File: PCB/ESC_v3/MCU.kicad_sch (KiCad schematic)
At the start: 40 parts, among them J10 Conn_01x01_Pin, J3 Conn_01x01_Pin, J4 Conn_01x01_Pin, J5 Conn_01x01_Pin, J6 Conn_01x01_Pin, J7 Conn_01x01_Pin, J8 Conn_01x01_Pin, J9 Conn_01x01_Pin, U5 STM32G431CBTx, Y2 16MHz

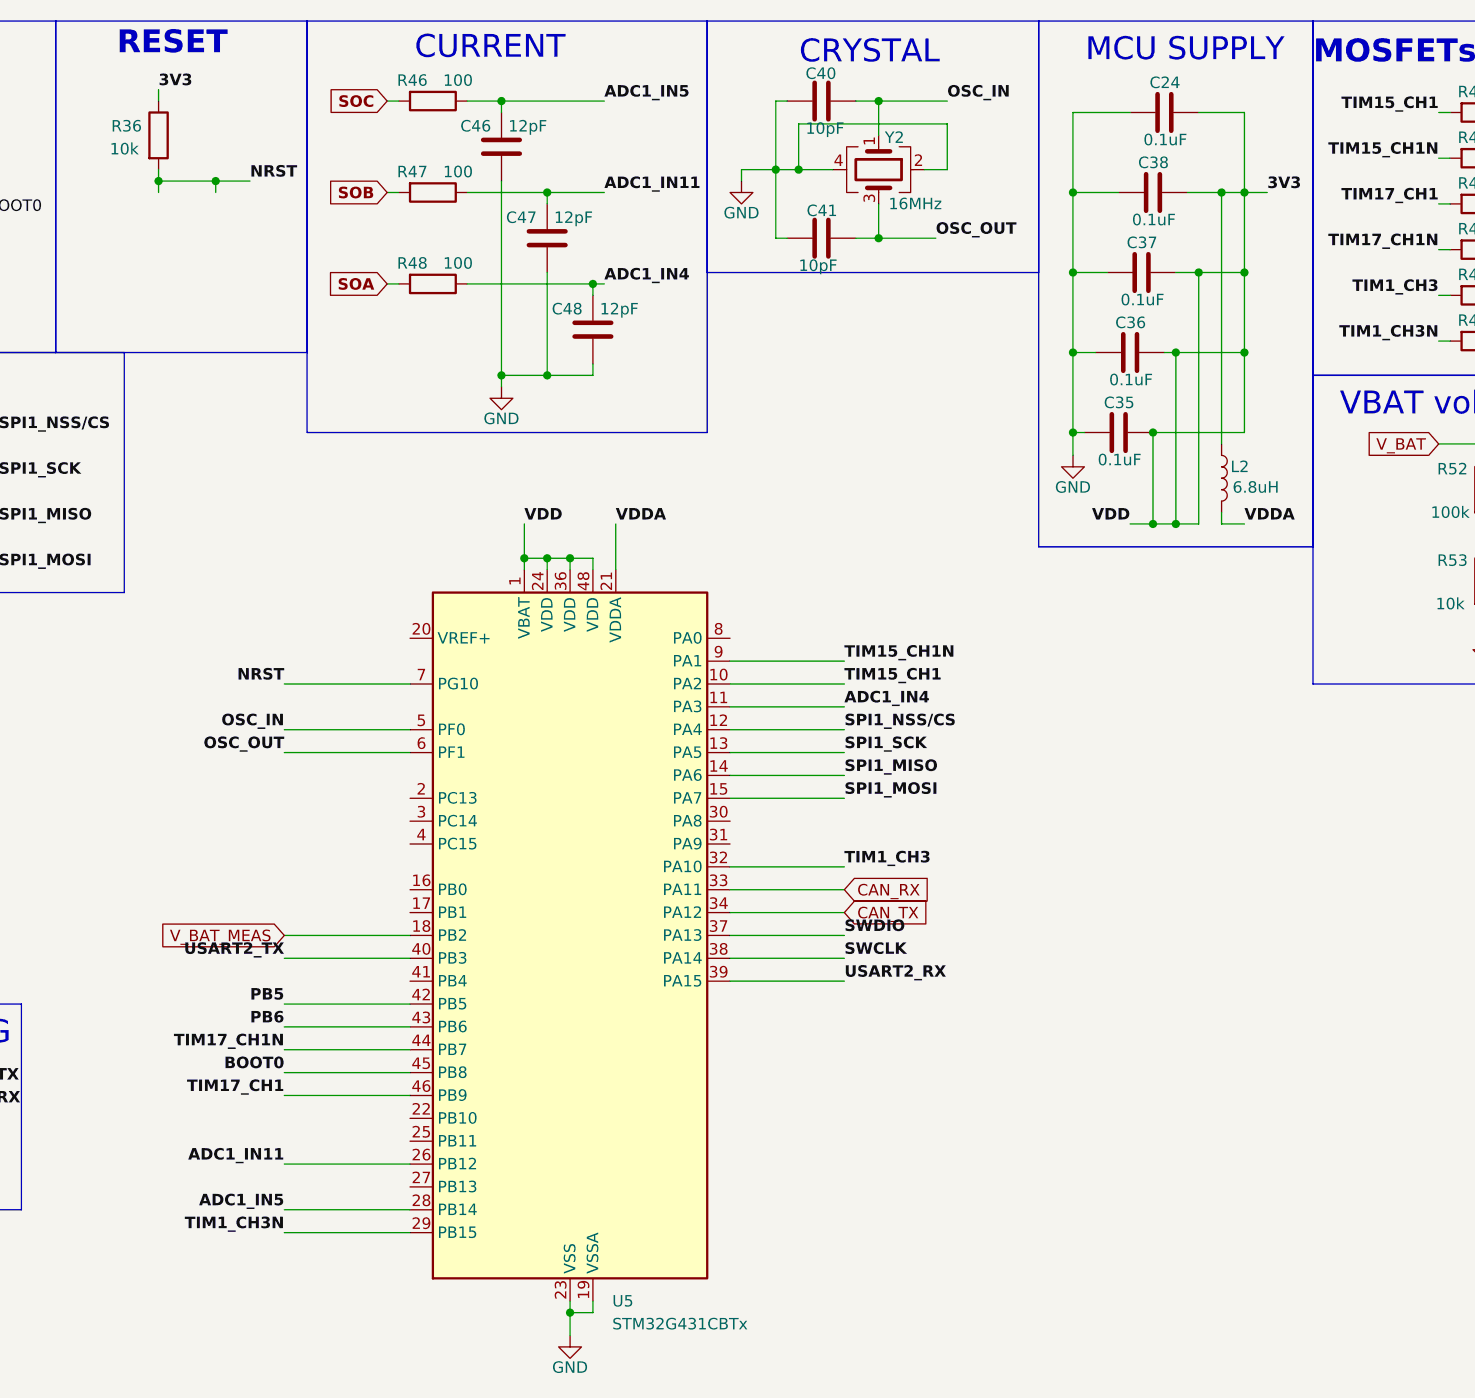
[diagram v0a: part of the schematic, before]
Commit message: Fix DRVR schematic wiring and PCB nets
Clean up DRVR.kicad_sch by adding/removing junctions and wires, rerouting traces and repositioning symbols; update component properties (capacitor values/ratings and label positions). Update ESC_v3.kicad_pcb to match schematic changes: reorder/renumber nets, correct pin/net assignments and adjust footprints/placements. Remove many outdated ESC_v3-backups ZIPs and add new timestamped backup ZIPs; add STM/STM.ioc and update MCU.kicad_sch and related project files. These changes correct net mappings and tidy schematic/PCB routing and metadata.
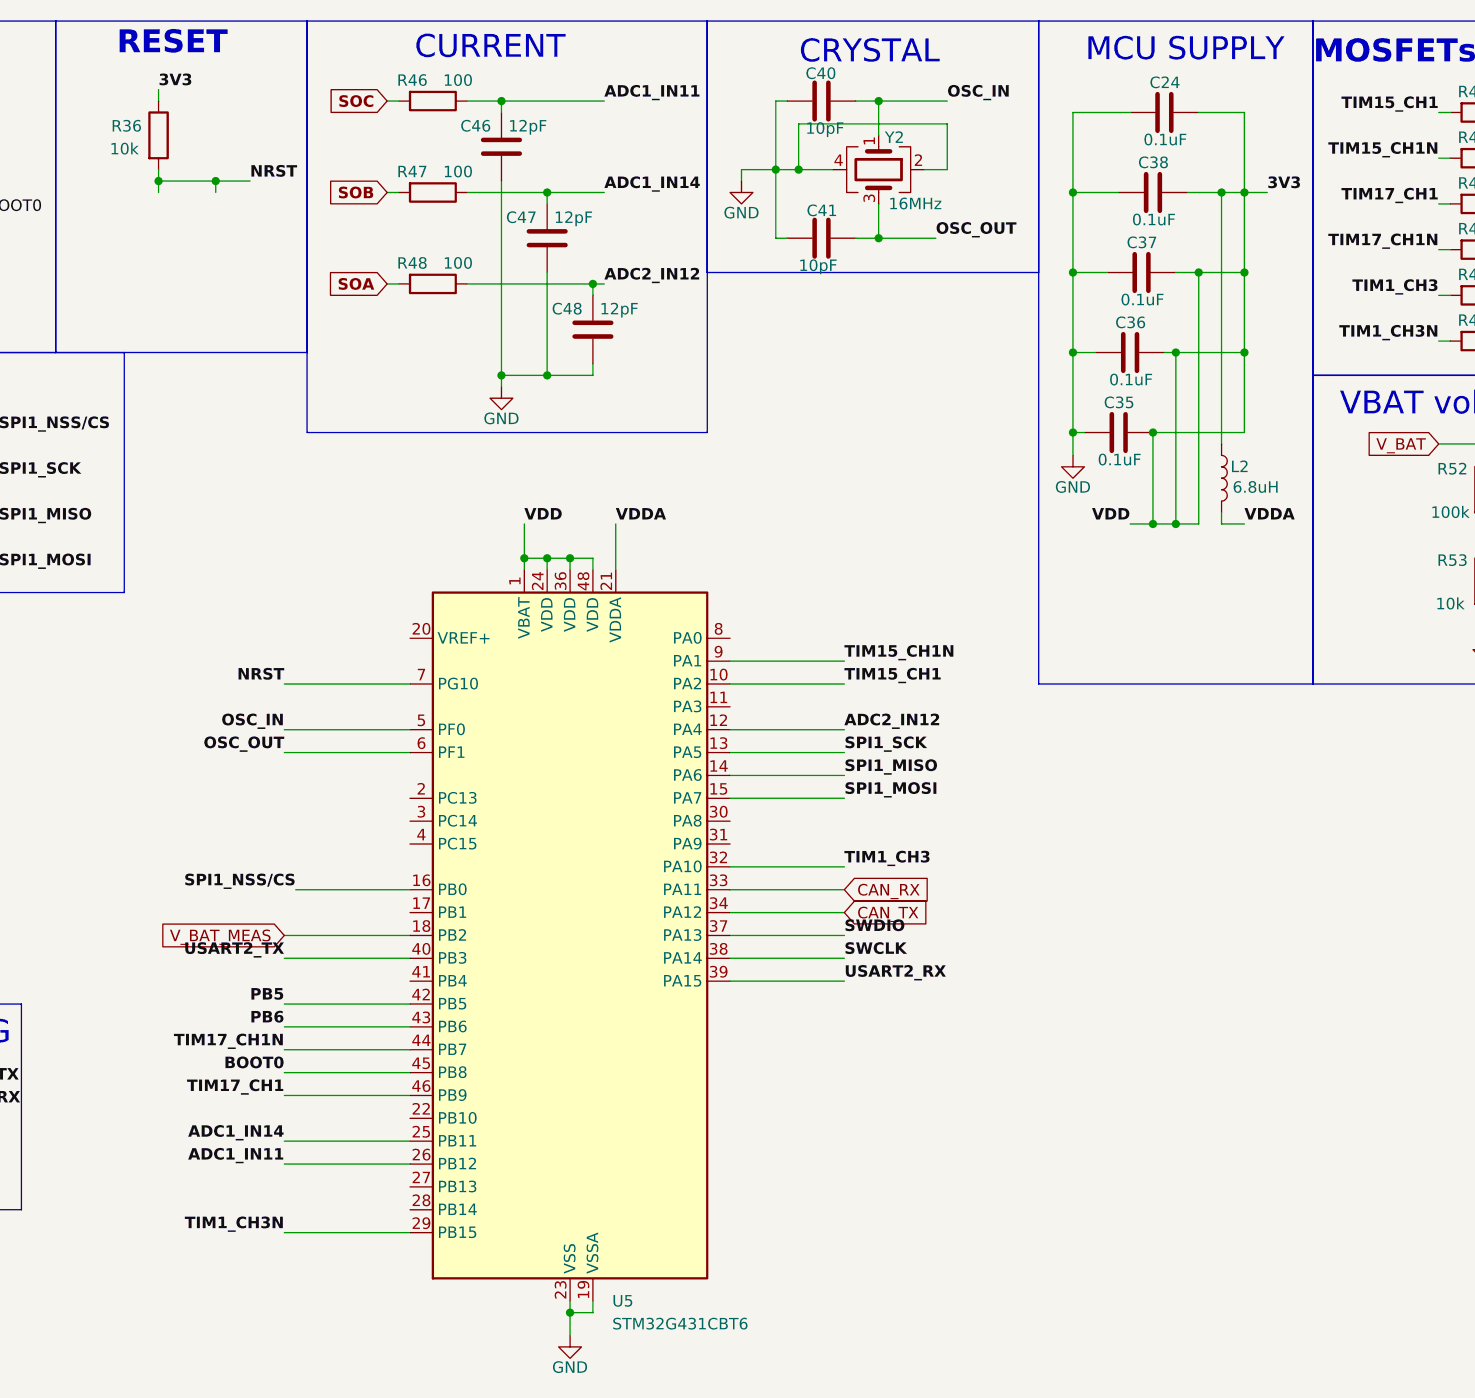
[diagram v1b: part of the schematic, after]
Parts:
- U5: value STM32G431CBTx -> STM32G431CBT6
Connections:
- net ADC1_IN11: now also C46.1, R46.1; no longer C47.1, R47.1
- net SPI1_NSS/CS: now also U5.16 (PB0); no longer U5.12 (PA4)
- net ADC1_IN14: now reaches U5.25 (PB11)
- net ADC1_IN14: now also C47.1, R47.1
- net ADC1_IN4 renamed ADC2_IN12
- net ADC2_IN12: now also U5.12 (PA4); no longer U5.11 (PA3)
- removed net ADC1_IN5: C46.1, R46.1, U5.28 (PB14)
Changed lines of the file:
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@@
 	(rectangle
 		(start 166.37 20.32)
-		(end 196.85 78.74)
+		(end 196.85 93.98)
 		(stroke
 			(width 0)
@@
 	(wire
 		(pts
-			(xy 82.55 147.32) (xy 96.52 147.32)
-		)
-		(stroke
-			(width 0)
-			(type default)
-		)
-	)
-	(wire
-		(pts
 			(xy 116.84 49.53) (xy 118.11 49.53)
 		)
@@
 	(wire
 		(pts
-			(xy 144.78 99.06) (xy 132.08 99.06)
-		)
-		(stroke
-			(width 0)
-			(type default)
-		)
-	)
-	(wire
-		(pts
 			(xy 43.18 95.25) (xy 39.37 95.25)
 		)
@@
 	(wire
 		(pts
+			(xy 82.55 144.78) (xy 96.52 144.78)
+		)
+		(stroke
+			(width 0)
+			(type default)
+		)
+	)
+	(wire
+		(pts
 			(xy 82.55 134.62) (xy 96.52 134.62)
 		)
@@
 	(wire
 		(pts
+			(xy 82.55 147.32) (xy 96.52 147.32)
+		)
+		(stroke
+			(width 0)
+			(type default)
+		)
+	)
+	(wire
+		(pts
 			(xy 82.55 139.7) (xy 96.52 139.7)
 		)
@@
 	(wire
 		(pts
+			(xy 83.82 116.84) (xy 96.52 116.84)
+		)
+		(stroke
+			(width 0)
+			(type default)
+		)
+	)
+	(wire
+		(pts
 			(xy 137.16 44.45) (xy 138.43 44.45)
 		)
@@
 	(wire
 		(pts
-			(xy 144.78 96.52) (xy 132.08 96.52)
-		)
-		(stroke
-			(width 0)
-			(type default)
-		)
-	)
-	(wire
-		(pts
 			(xy 39.37 50.8) (xy 39.37 52.07)
 		)
@@
 	(wire
 		(pts
-			(xy 82.55 152.4) (xy 96.52 152.4)
+			(xy 186.69 76.2) (xy 189.23 76.2)
 		)
 		(stroke
@@
 	(wire
 		(pts
-			(xy 186.69 76.2) (xy 189.23 76.2)
+			(xy 41.91 138.43) (xy 39.37 138.43)
 		)
 		(stroke
@@
 	(wire
 		(pts
-			(xy 41.91 138.43) (xy 39.37 138.43)
+			(xy 223.52 86.36) (xy 223.52 87.63)
 		)
 		(stroke
@@
 	(wire
 		(pts
-			(xy 223.52 86.36) (xy 223.52 87.63)
+			(xy 40.64 66.04) (xy 41.91 66.04)
 		)
 		(stroke
@@
 	(wire
 		(pts
-			(xy 40.64 66.04) (xy 41.91 66.04)
+			(xy 148.59 44.45) (xy 154.94 44.45)
 		)
 		(stroke
@@
 	(wire
 		(pts
-			(xy 148.59 44.45) (xy 154.94 44.45)
+			(xy 144.78 93.98) (xy 132.08 93.98)
 		)
 		(stroke
@@
 	(wire
 		(pts
-			(xy 144.78 93.98) (xy 132.08 93.98)
+			(xy 144.78 99.06) (xy 132.08 99.06)
 		)
 		(stroke
@@
 		)
 	)
+	(label "SPI1_NSS{slash}CS"
+		(at 83.82 116.84 180)
+		(effects
+			(font
+				(size 1.27 1.27)
+				(thickness 0.254)
+				(bold yes)
+			)
+			(justify right bottom)
+		)
+	)
 	(label "TIM17_CH1N"
 		(at 82.55 134.62 180)
@@
 		)
 	)
-	(label "ADC1_IN4"
+	(label "ADC2_IN12"
+		(at 144.78 99.06 0)
+		(effects
+			(font
+				(size 1.27 1.27)
+				(thickness 0.254)
+				(bold yes)
+			)
+			(justify left bottom)
+		)
+	)
+	(label "ADC2_IN12"
 		(at 118.11 49.53 0)
 		(effects
@@
 		)
 	)
-	(label "ADC1_IN5"
+	(label "ADC1_IN11"
 		(at 118.11 29.21 0)
 		(effects
@@
 		)
 	)
-	(label "ADC1_IN5"
-		(at 82.55 152.4 180)
+	(label "SPI1_MOSI"
+		(at 50.8 81.28 0)
 		(effects
 			(font
@@
 				(bold yes)
 			)
-			(justify right bottom)
+			(justify left bottom)
 		)
 	)
-	(label "SPI1_MOSI"
-		(at 50.8 81.28 0)
+	(label "ADC1_IN14"
+		(at 82.55 144.78 180)
 		(effects
 			(font
@@
 				(bold yes)
 			)
-			(justify left bottom)
+			(justify right bottom)
 		)
 	)
@@
 		)
 	)
-	(label "ADC1_IN11"
+	(label "ADC1_IN14"
 		(at 118.11 39.37 0)
 		(effects
@@
 		)
 	)
-	(label "SPI1_NSS{slash}CS"
-		(at 144.78 99.06 0)
-		(effects
-			(font
-				(size 1.27 1.27)
-				(thickness 0.254)
-				(bold yes)
-			)
-			(justify left bottom)
-		)
-	)
 	(label "TIM1_CH3N"
 		(at 210.82 55.88 180)
@@
 		)
 	)
+	(label "ADC1_IN11"
+		(at 82.55 147.32 180)
+		(effects
+			(font
+				(size 1.27 1.27)
+				(thickness 0.254)
+				(bold yes)
+			)
+			(justify right bottom)
+		)
+	)
 	(label "TIM15_CH1N"
 		(at 210.82 35.56 180)
@@
 		)
 	)
-	(label "ADC1_IN11"
-		(at 82.55 147.32 180)
-		(effects
-			(font
-				(size 1.27 1.27)
-				(thickness 0.254)
-				(bold yes)
-			)
-			(justify right bottom)
-		)
-	)
 	(label "TIM15_CH1N"
 		(at 144.78 91.44 0)
@@
 		)
 	)
-	(label "ADC1_IN4"
-		(at 144.78 96.52 0)
-		(effects
-			(font
-				(size 1.27 1.27)
-				(thickness 0.254)
-				(bold yes)
-			)
-			(justify left bottom)
-		)
-	)
 	(label "PB5"
 		(at 45.72 127 0)
@@
 			)
 		)
-		(property "Value" "STM32G431CBTx"
+		(property "Value" "STM32G431CBT6"
 			(at 118.9833 165.1 0)
 			(effects

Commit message: Updates
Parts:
- added C33, C43: 100n, Capacitor_SMD:C_0805_2012Metric, symbol Device:C
- added C39, C42: 1u/DNP, Capacitor_SMD:C_0805_2012Metric, symbol Device:C
- C24, C36, C37: value 0.1uF -> 100n
- C35: value 0.1uF -> 10n
- C38: value 0.1uF -> 4u7
- C40, C41: value 10pF -> 6p8
- Y2: value 16MHz -> 24MHz
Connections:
- net 3V3: now also L2.2, C42.2; no longer C35.2, L2.1
- net CAL_DV: now also U5.27 (PB13)
- net GND: now also C33.2, C39.1, C42.1, C43.1
- net NRST: now also C33.1
- net VDDA: now also C35.2, L2.1, U5.20 (VREF+), C39.2, C43.2; no longer L2.2
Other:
- note added: "From STM's G4 Nucleo Board Schematic"
- note added: "Maybe: Ferrite bead 600 Ω @ 100 MHz, low DC resistance (Murata BLM18 / BLM21 series)"
- moved on the sheet: C24, C32, C35, C36, C37, C38, C41, L2, R35, R40, R41, R42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

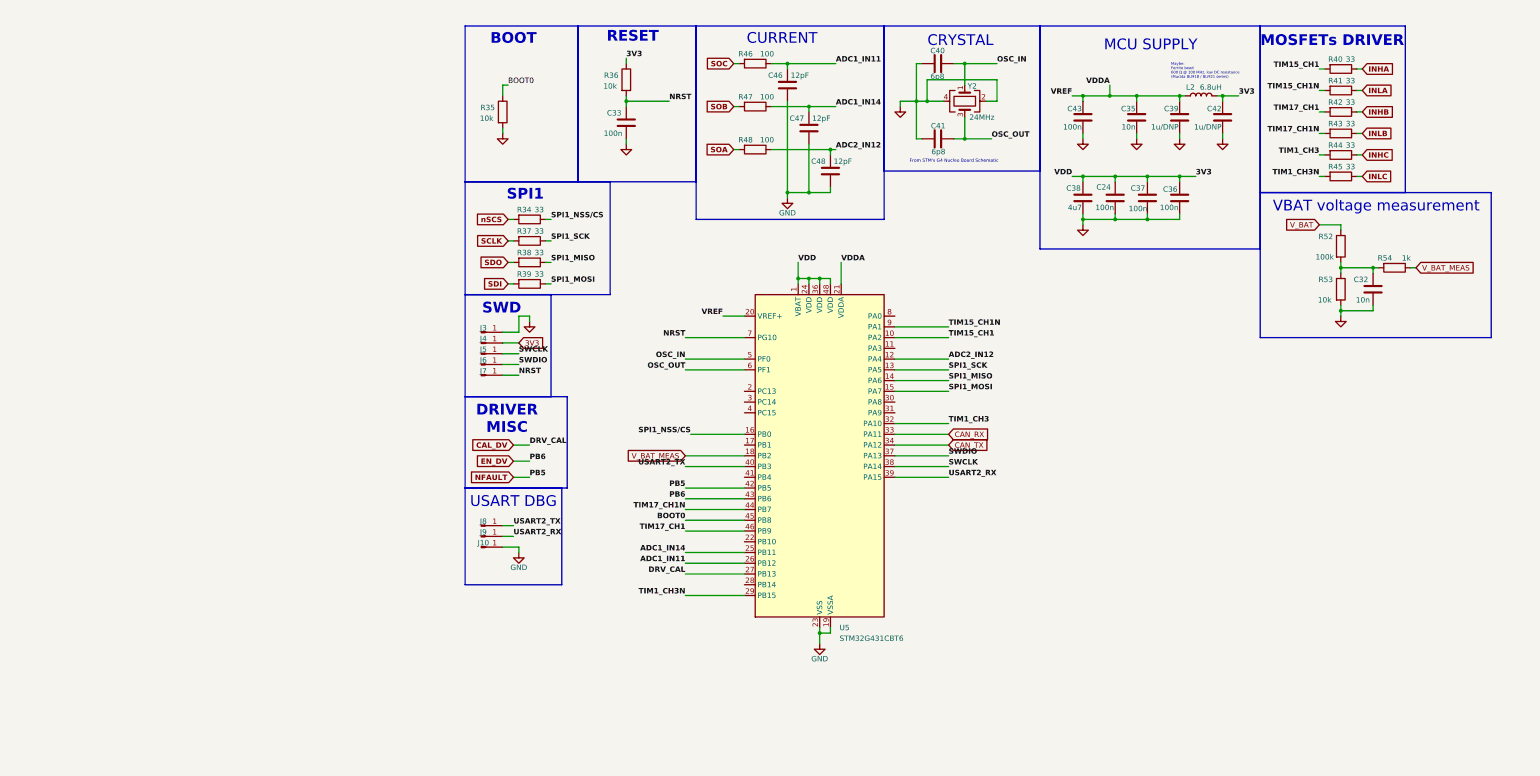
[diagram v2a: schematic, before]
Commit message: Update PCB layout and driver schematic
Adjust KiCad project files: many PCB footprint positions/rotations/uuids and silk/pad orientations updated, trace segments and widths adjusted, vias added/moved (several tented/free vias), and zone_connect enabled on referenced footprints. Correct MCU pin net assignments (PB4/PB5/PB6 / NFAULT / EN_DV) and other net fixes. In DRVR schematic change stroke styles to dashed and update a capacitor value from ">=10uF" to "22u". Remove several old backup zip files and add new backup snapshots. Miscellaneous small .kicad_prl/.kicad_sch/.ioc updates included for consistency and routing cleanup.
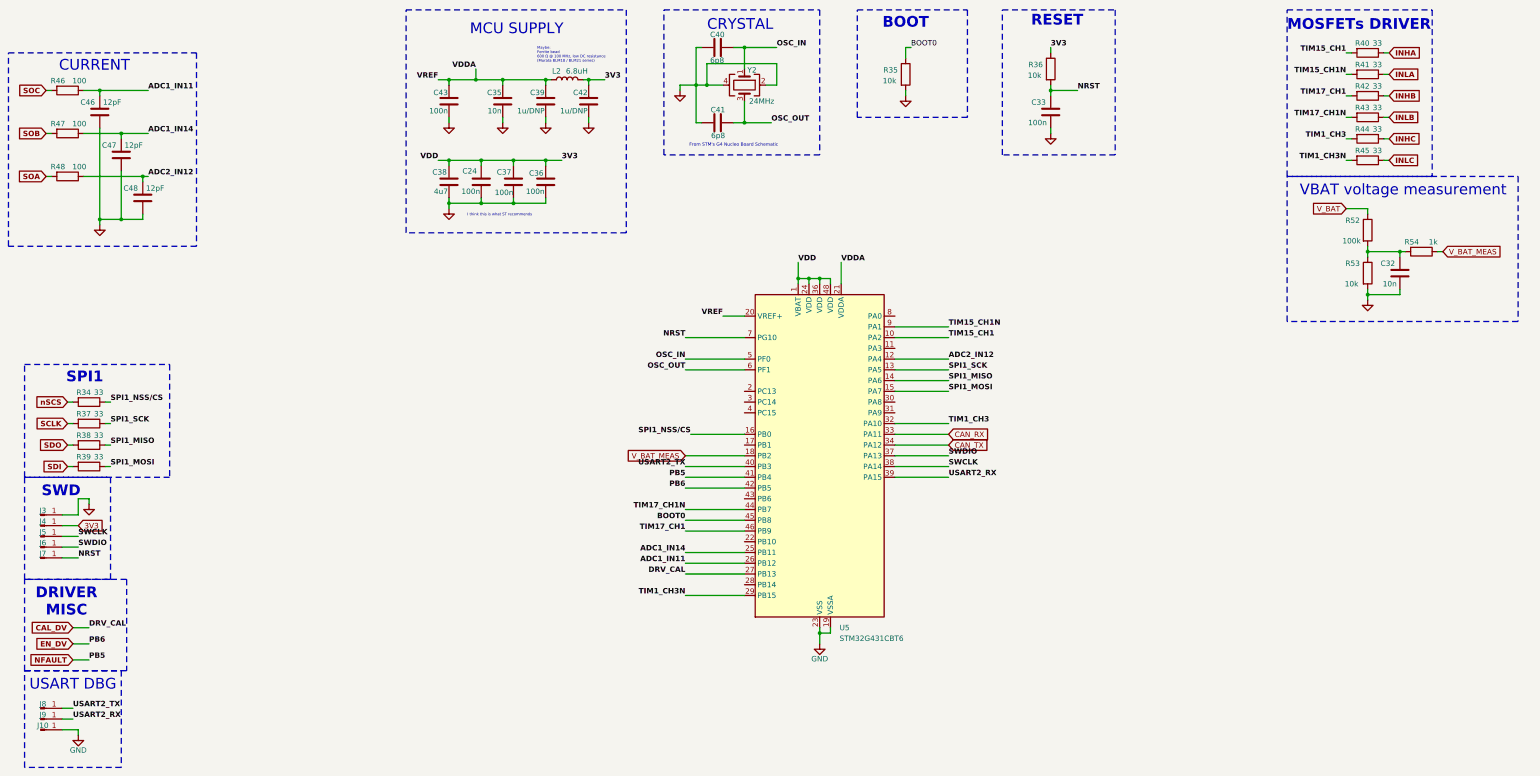
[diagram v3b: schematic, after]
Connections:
- net EN_DV: now also U5.42 (PB5); no longer U5.43 (PB6)
- net NFAULT: now also U5.41 (PB4); no longer U5.42 (PB5)
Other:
- note added: "I think this is what ST recommends"
- moved on the sheet: C24, C32, C33, C35, C36, C37, C38, C39, C40, C41, C42, C43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
